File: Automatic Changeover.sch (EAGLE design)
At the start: 44 parts, among them IC1 ACS750LCA-050, IC2 XMEGA16A4A, IC3 XMEGA16A4A, IC4 ACS750LCA-050, IC5 ACS750LCA-050, K1 S216SE1, K2 S216SE1, K3 S216SE1, K4 S216SE1, K5 S216SE1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

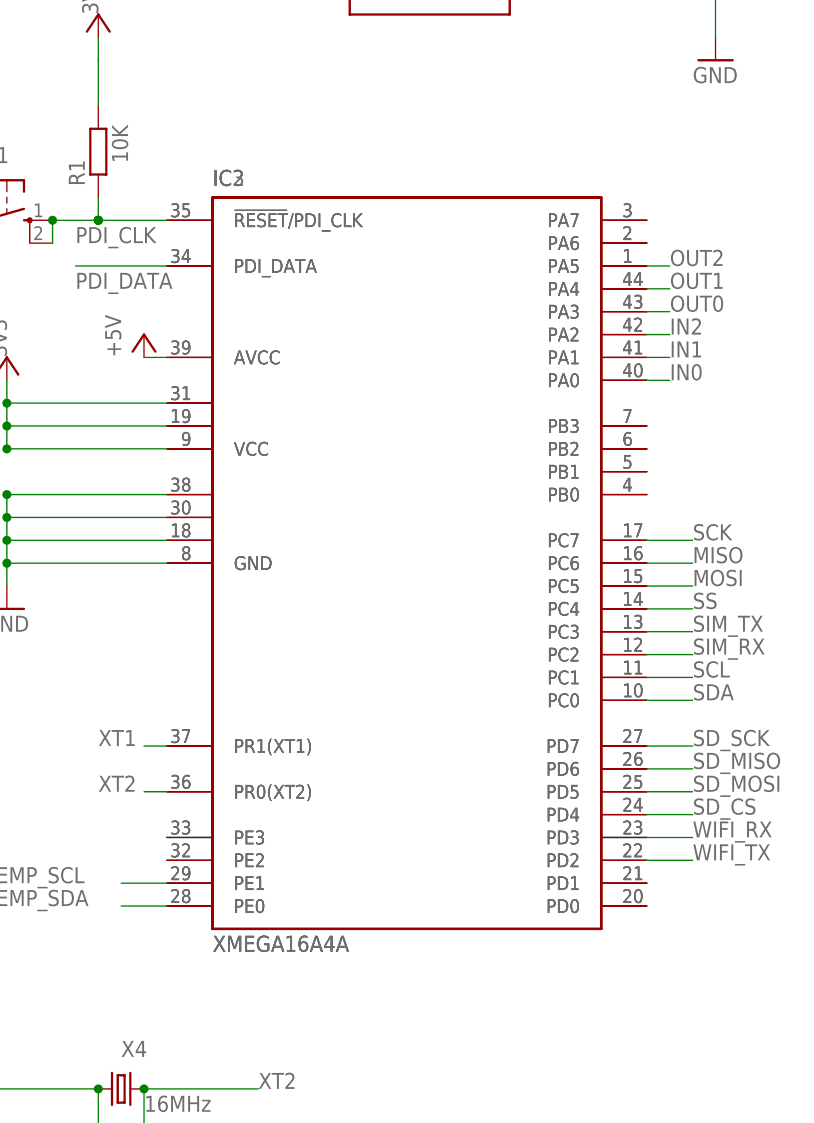
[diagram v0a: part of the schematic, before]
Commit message: corrected an error in schematic
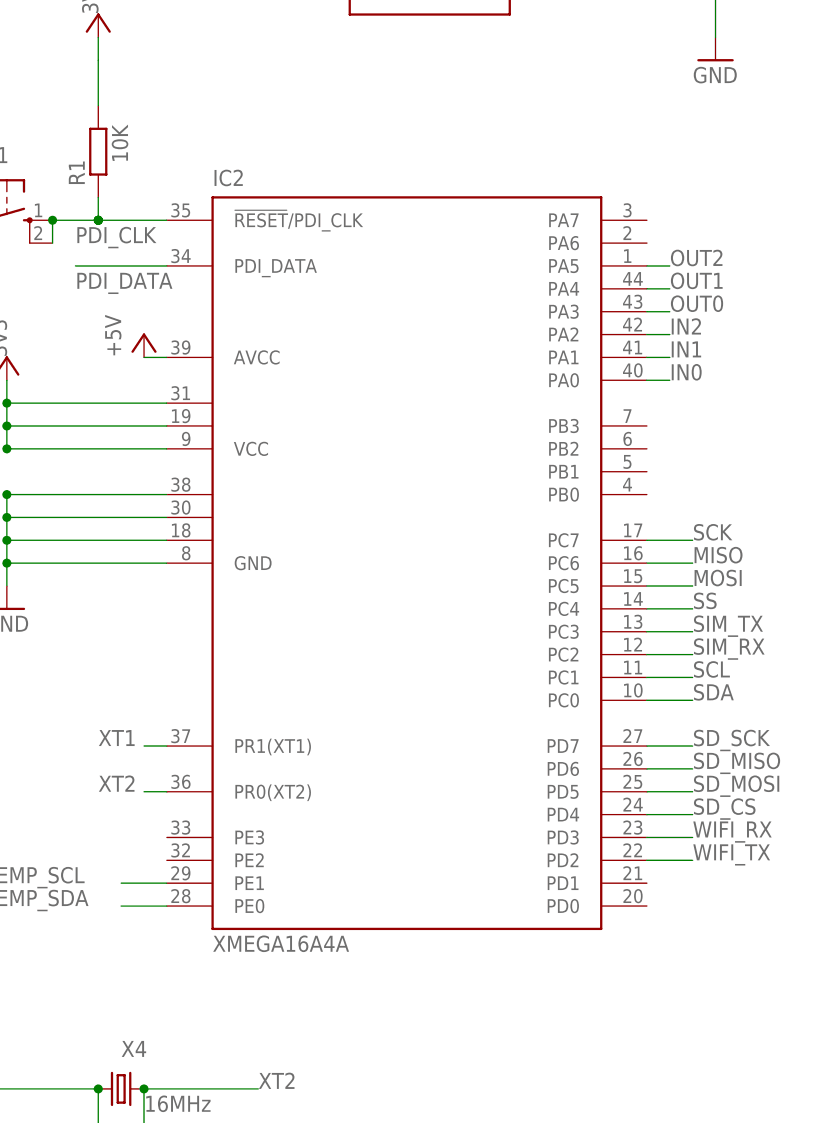
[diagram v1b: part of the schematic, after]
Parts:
- removed IC3: XMEGA16A4A, atmel:XMEGA16A4A
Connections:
- removed net N$12: IC2.PD1, IC3.PD1
- removed net N$13: IC2.PD0, IC3.PD0
- removed net N$22: IC2.PB3, IC3.PB3
- removed net N$23: IC2.PB2, IC3.PB2
- removed net N$24: IC2.PB1, IC3.PB1
- removed net N$25: IC2.PB0, IC3.PB0
- removed net N$26: IC2.PA6, IC3.PA6
- removed net N$27: IC2.PA7, IC3.PA7
- removed net N$4: IC2.PE2, IC3.PE2
- removed net N$5: IC2.PE3, IC3.PE3
- net +5V: no longer IC3.AVCC
- net GND: no longer IC3.GND, IC3.GND1, IC3.GND2, IC3.GND3
- net IN0: no longer IC3.PA0
- net IN1: no longer IC3.PA1
- net IN2: no longer IC3.PA2
- net MISO: no longer IC3.PC6
- net MOSI: no longer IC3.PC5
- net OUT0: no longer IC3.PA3
- net OUT1: no longer IC3.PA4
- net OUT2: no longer IC3.PA5
- net PDI_CLK: no longer IC3.!RESET!/PDI_CLK
- net PDI_DATA: no longer IC3.PDI_DATA
- net SCK: no longer IC3.PC7
- net SCL: no longer IC3.PC1
- net SDA: no longer IC3.PC0
- net SD_CS: no longer IC3.PD4
- net SD_MISO: no longer IC3.PD6
- net SD_MOSI: no longer IC3.PD5
- net SD_SCK: no longer IC3.PD7
- net SIM_RX: no longer IC3.PC2
- net SIM_TX: no longer IC3.PC3
- net SS: no longer IC3.PC4
- net TEMP_SCL: no longer IC3.PE1
- net TEMP_SDA: no longer IC3.PE0
- net VCC: no longer IC3.VCC, IC3.VCC1, IC3.VCC2
- net WIFI_RX: no longer IC3.PD3
- net WIFI_TX: no longer IC3.PD2
- net XT1: no longer IC3.PR1(XT1)
- net XT2: no longer IC3.PR0(XT2)

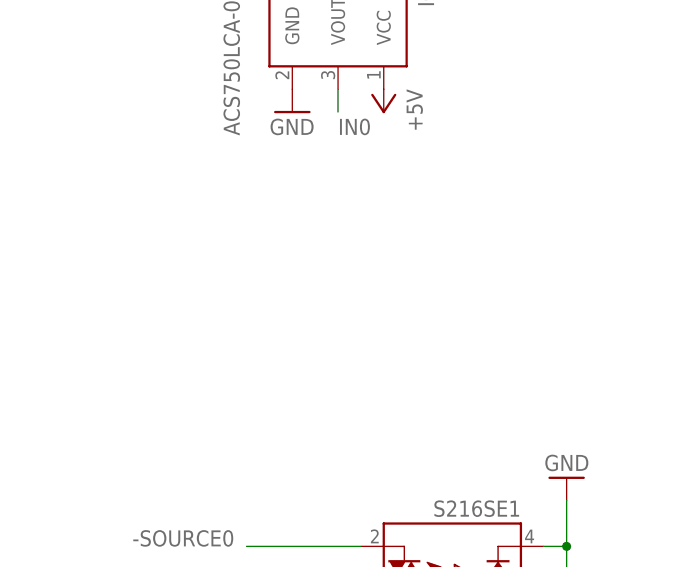
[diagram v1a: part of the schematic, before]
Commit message: add pad through hole for power source connection
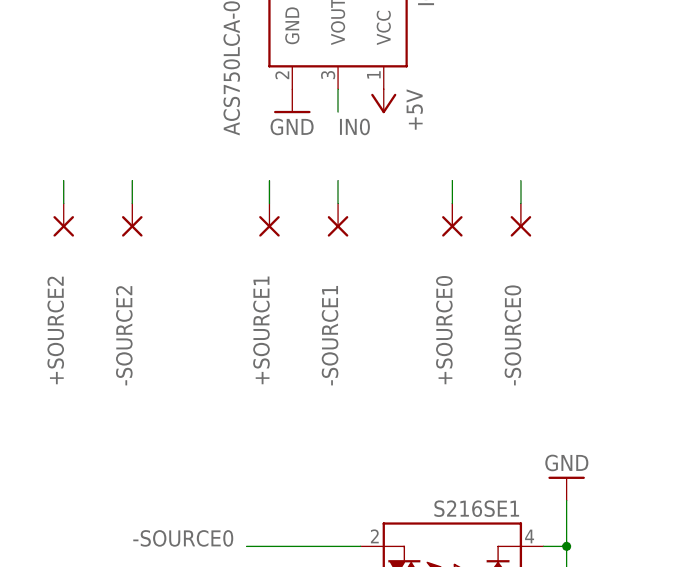
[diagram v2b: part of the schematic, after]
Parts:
- added +SOURCE0, +SOURCE1, +SOURCE2, -SOURCE0, -SOURCE1, -SOURCE2: (no value), wirepad:3,81/1,4
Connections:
- net +SOURCE0: now also +SOURCE0.P
- net +SOURCE1: now also +SOURCE1.P
- net +SOURCE2: now also +SOURCE2.P
- net -SOURCE0: now also -SOURCE0.P
- net -SOURCE1: now also -SOURCE1.P
- net -SOURCE2: now also -SOURCE2.P
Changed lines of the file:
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@@
 <part name="GND22" library="supply1" library_urn="urn:adsk.eagle:library:371" deviceset="GND" device=""/>
 <part name="P+11" library="supply1" library_urn="urn:adsk.eagle:library:371" deviceset="VCC" device="" value="3V3"/>
+<part name="-SOURCE0" library="wirepad" library_urn="urn:adsk.eagle:library:412" deviceset="3,81/1,4" device="" package3d_urn="urn:adsk.eagle:package:30835/1"/>
+<part name="+SOURCE0" library="wirepad" library_urn="urn:adsk.eagle:library:412" deviceset="3,81/1,4" device="" package3d_urn="urn:adsk.eagle:package:30835/1"/>
+<part name="-SOURCE1" library="wirepad" library_urn="urn:adsk.eagle:library:412" deviceset="3,81/1,4" device="" package3d_urn="urn:adsk.eagle:package:30835/1"/>
+<part name="+SOURCE1" library="wirepad" library_urn="urn:adsk.eagle:library:412" deviceset="3,81/1,4" device="" package3d_urn="urn:adsk.eagle:package:30835/1"/>
+<part name="+SOURCE2" library="wirepad" library_urn="urn:adsk.eagle:library:412" deviceset="3,81/1,4" device="" package3d_urn="urn:adsk.eagle:package:30835/1"/>
+<part name="-SOURCE2" library="wirepad" library_urn="urn:adsk.eagle:library:412" deviceset="3,81/1,4" device="" package3d_urn="urn:adsk.eagle:package:30835/1"/>
 </parts>
 <sheets>
@@
 <instance part="P+11" gate="VCC" x="-43.18" y="-78.74" smashed="yes" rot="R180">
 <attribute name="VALUE" x="-45.72" y="-71.12" size="1.778" layer="96" rot="R270"/>
+</instance>
+<instance part="-SOURCE0" gate="1" x="-93.98" y="25.4" smashed="yes" rot="R90">
+<attribute name="VALUE" x="-90.678" y="24.257" size="1.778" layer="96" rot="R90"/>
+</instance>
+<instance part="+SOURCE0" gate="1" x="-101.6" y="25.4" smashed="yes" rot="R90">
+<attribute name="VALUE" x="-98.298" y="24.257" size="1.778" layer="96" rot="R90"/>
+</instance>
+<instance part="-SOURCE1" gate="1" x="-114.3" y="25.4" smashed="yes" rot="R90">
+<attribute name="VALUE" x="-110.998" y="24.257" size="1.778" layer="96" rot="R90"/>
+</instance>
+<instance part="+SOURCE1" gate="1" x="-121.92" y="25.4" smashed="yes" rot="R90">
+<attribute name="VALUE" x="-118.618" y="24.257" size="1.778" layer="96" rot="R90"/>
+</instance>
+<instance part="+SOURCE2" gate="1" x="-144.78" y="25.4" smashed="yes" rot="R90">
+<attribute name="VALUE" x="-141.478" y="24.257" size="1.778" layer="96" rot="R90"/>
+</instance>
+<instance part="-SOURCE2" gate="1" x="-137.16" y="25.4" smashed="yes" rot="R90">
+<attribute name="VALUE" x="-133.858" y="24.257" size="1.778" layer="96" rot="R90"/>
 </instance>
 </instances>
@@
 <label x="-137.16" y="-10.16" size="1.778" layer="95"/>
 </segment>
+<segment>
+<pinref part="-SOURCE0" gate="1" pin="P"/>
+<wire x1="-93.98" y1="27.94" x2="-93.98" y2="30.48" width="0.1524" layer="91"/>
+<label x="-93.98" y="7.62" size="1.778" layer="95" rot="R90"/>
+</segment>
 </net>
 <net name="+SOURCE0" class="0">
@@
 <wire x1="-111.76" y1="-27.94" x2="-124.46" y2="-27.94" width="0.1524" layer="91"/>
 <label x="-137.16" y="-27.94" size="1.778" layer="95"/>
+</segment>
+<segment>
+<pinref part="+SOURCE0" gate="1" pin="P"/>
+<wire x1="-101.6" y1="27.94" x2="-101.6" y2="30.48" width="0.1524" layer="91"/>
+<label x="-101.6" y="7.62" size="1.778" layer="95" rot="R90"/>
 </segment>
 </net>
@@
 <label x="-149.86" y="88.9" size="1.778" layer="95"/>
 </segment>
+<segment>
+<pinref part="-SOURCE1" gate="1" pin="P"/>
+<wire x1="-114.3" y1="27.94" x2="-114.3" y2="30.48" width="0.1524" layer="91"/>
+<label x="-114.3" y="7.62" size="1.778" layer="95" rot="R90"/>
+</segment>
 </net>
 <net name="+SOURCE1" class="0">
@@
 <label x="-149.86" y="73.66" size="1.778" layer="95"/>
 </segment>
+<segment>
+<pinref part="+SOURCE1" gate="1" pin="P"/>
+<wire x1="-121.92" y1="27.94" x2="-121.92" y2="30.48" width="0.1524" layer="91"/>
+<label x="-121.92" y="7.62" size="1.778" layer="95" rot="R90"/>
+</segment>
 </net>
 <net name="-SOURCE2" class="0">
@@
 <label x="-149.86" y="106.68" size="1.778" layer="95"/>
 </segment>
+<segment>
+<pinref part="-SOURCE2" gate="1" pin="P"/>
+<wire x1="-137.16" y1="27.94" x2="-137.16" y2="30.48" width="0.1524" layer="91"/>
+<label x="-137.16" y="7.62" size="1.778" layer="95" rot="R90"/>
+</segment>
 </net>
 <net name="+SOURCE2" class="0">
@@
 <label x="-149.86" y="93.98" size="1.778" layer="95"/>
 </segment>
-</net>
+<segment>
+<pinref part="+SOURCE2" gate="1" pin="P"/>
+<wire x1="-144.78" y1="27.94" x2="-144.78" y2="30.48" width="0.1524" layer="91"/>
+<label x="-144.78" y="7.62" size="1.778" layer="95" rot="R90"/>
+</segment>
+</net>

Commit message: adjusted many components to desired position
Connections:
- removed net N$15: C3.2
- net GND: now also C3.2
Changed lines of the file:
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@@
 <attribute name="VALUE" x="7.62" y="63.5" size="1.778" layer="96" rot="R90"/>
 </instance>
-<instance part="GND9" gate="1" x="2.54" y="48.26" smashed="yes">
-<attribute name="VALUE" x="0" y="45.72" size="1.778" layer="96"/>
+<instance part="GND9" gate="1" x="2.54" y="45.72" smashed="yes">
+<attribute name="VALUE" x="0" y="43.18" size="1.778" layer="96"/>
 </instance>
 <instance part="GND7" gate="1" x="-7.62" y="17.78" smashed="yes">
@@
 <wire x1="157.48" y1="-35.56" x2="167.64" y2="-35.56" width="0.1524" layer="91"/>
 <pinref part="P+2" gate="1" pin="+5V"/>
+<label x="154.94" y="-30.48" size="1.778" layer="95"/>
 </segment>
 <segment>
@@
 <wire x1="2.54" y1="60.96" x2="10.16" y2="60.96" width="0.1524" layer="91"/>
 <junction x="2.54" y="60.96"/>
+<label x="12.7" y="63.5" size="1.778" layer="95"/>
 </segment>
 <segment>
@@
 <wire x1="-71.12" y1="-15.24" x2="-63.5" y2="-15.24" width="0.1524" layer="91"/>
 <junction x="-63.5" y="-15.24"/>
+<label x="-60.96" y="-7.62" size="1.778" layer="95"/>
 </segment>
 <segment>
@@
 <junction x="43.18" y="-12.7"/>
 <junction x="43.18" y="-5.08"/>
+<label x="35.56" y="-17.78" size="1.778" layer="95"/>
 </segment>
 <segment>
@@
 <wire x1="38.1" y1="22.86" x2="38.1" y2="25.4" width="0.1524" layer="91"/>
 <junction x="38.1" y="25.4"/>
+<label x="27.94" y="20.32" size="1.778" layer="95"/>
 </segment>
 <segment>
@@
 <wire x1="58.42" y1="-83.82" x2="55.88" y2="-83.82" width="0.1524" layer="91"/>
 <junction x="55.88" y="-83.82"/>
+<label x="58.42" y="-86.36" size="1.778" layer="95"/>
 </segment>
 <segment>
@@
 <pinref part="GND4" gate="1" pin="GND"/>
 <pinref part="JP1" gate="G$1" pin="6"/>
+<label x="203.2" y="-68.58" size="1.778" layer="95"/>
 </segment>
 <segment>
@@
 <pinref part="U$1" gate="G$1" pin="6"/>
 <wire x1="157.48" y1="-40.64" x2="167.64" y2="-40.64" width="0.1524" layer="91"/>
+<label x="147.32" y="-48.26" size="1.778" layer="95"/>
 </segment>
 <segment>
@@
 <wire x1="-7.62" y1="21.844" x2="-7.62" y2="22.86" width="0.1524" layer="91"/>
 <junction x="-7.62" y="22.86"/>
+<label x="-2.54" y="17.78" size="1.778" layer="95"/>
 </segment>
 <segment>
@@
 <wire x1="-27.94" y1="55.88" x2="-27.94" y2="45.72" width="0.1524" layer="91"/>
 <pinref part="GND8" gate="1" pin="GND"/>
+<label x="-25.4" y="43.18" size="1.778" layer="95"/>
 </segment>
 <segment>
@@
 <wire x1="101.6" y1="116.84" x2="101.6" y2="104.14" width="0.1524" layer="91"/>
 <junction x="101.6" y="104.14"/>
+<label x="104.14" y="91.44" size="1.778" layer="95"/>
 </segment>
 <segment>
@@
 <pinref part="U$8" gate="G$1" pin="GND"/>
 <wire x1="119.38" y1="101.6" x2="134.62" y2="101.6" width="0.1524" layer="91"/>
+<label x="121.92" y="88.9" size="1.778" layer="95"/>
 </segment>
 <segment>
@@
 <wire x1="205.74" y1="55.88" x2="205.74" y2="38.1" width="0.1524" layer="91"/>
 <junction x="205.74" y="38.1"/>
+<label x="208.28" y="33.02" size="1.778" layer="95"/>
 </segment>
 <segment>
@@
 <wire x1="104.14" y1="58.42" x2="121.92" y2="58.42" width="0.1524" layer="91"/>
 <wire x1="121.92" y1="58.42" x2="121.92" y2="45.72" width="0.1524" layer="91"/>
+<label x="124.46" y="45.72" size="1.778" layer="95"/>
 </segment>
 <segment>
@@
 <pinref part="GND17" gate="1" pin="GND"/>
 <wire x1="-35.56" y1="104.14" x2="-35.56" y2="99.06" width="0.1524" layer="91"/>
+<label x="-43.18" y="99.06" size="1.778" layer="95"/>
 </segment>
 <segment>
@@
 <pinref part="GND18" gate="1" pin="GND"/>
 <wire x1="0" y1="104.14" x2="0" y2="99.06" width="0.1524" layer="91"/>
+<label x="2.54" y="96.52" size="1.778" layer="95"/>
 </segment>
 <segment>
@@
 <wire x1="-88.9" y1="-5.08" x2="-88.9" y2="-10.16" width="0.1524" layer="91"/>
 <junction x="-88.9" y="-10.16"/>
+<label x="-86.36" y="-5.08" size="1.778" layer="95"/>
 </segment>
 <segment>
@@
 <wire x1="-86.36" y1="-45.72" x2="-86.36" y2="-48.26" width="0.1524" layer="91"/>
 <junction x="-86.36" y="-48.26"/>
+<label x="-83.82" y="-43.18" size="1.778" layer="95"/>
 </segment>
 <segment>
@@
 <wire x1="-86.36" y1="-83.82" x2="-86.36" y2="-86.36" width="0.1524" layer="91"/>
 <junction x="-86.36" y="-86.36"/>
+<label x="-83.82" y="-83.82" size="1.778" layer="95"/>
 </segment>
 <segment>
@@
 <wire x1="-35.56" y1="-76.2" x2="-35.56" y2="-60.96" width="0.1524" layer="91"/>
 <wire x1="-35.56" y1="-60.96" x2="-27.94" y2="-60.96" width="0.1524" layer="91"/>
+<label x="-35.56" y="-76.2" size="1.778" layer="95"/>
 </segment>
 <segment>
@@
 <wire x1="10.16" y1="-73.66" x2="10.16" y2="-60.96" width="0.1524" layer="91"/>
 <wire x1="10.16" y1="-60.96" x2="2.54" y2="-60.96" width="0.1524" layer="91"/>
+<label x="2.54" y="-73.66" size="1.778" layer="95"/>
+</segment>
+<segment>
+<pinref part="C3" gate="G$1" pin="2"/>
+<pinref part="GND9" gate="1" pin="GND"/>
+<wire x1="2.54" y1="48.26" x2="2.54" y2="50.8" width="0.1524" layer="91"/>
+<label x="5.08" y="45.72" size="1.778" layer="95"/>
 </segment>
 </net>
@@
 </segment>
 </net>
-<net name="N$15" class="0">
-<segment>
-<pinref part="C3" gate="G$1" pin="2"/>
-<pinref part="GND9" gate="1" pin="GND"/>
-</segment>
-</net>
